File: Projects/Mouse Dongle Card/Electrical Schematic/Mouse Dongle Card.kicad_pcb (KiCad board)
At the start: 2 copper layers, 26 x 27.9 mm, 11 parts, among them P1 USB_C_Plug_USB2.0, U1 AP2112K-3.3

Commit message: Started work on USB Dongle Card
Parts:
- removed C2: 10uF, Capacitor_SMD:C_0805_2012Metric
- removed R1: 5.1k, Resistor_SMD:R_0603_1608Metric
- removed U1: AP2112K-3.3, Package_TO_SOT_SMD:SOT-23-5
- added R2: 5.1k, Resistor_SMD:R_1206_3216Metric_Pad1.30x1.75mm_HandSolder, F.Cu at (100.1, 123.5)
- added USBSolder1: ~, Connector_USB_PCB_Edge:USB_A_PCB_Edge_receptacle, B.Cu at (108.3, 128.6)
- C1: value 10uF -> 10nF; footprint Capacitor_SMD:C_0805_2012Metric -> Capacitor_SMD:C_1206_3216Metric_Pad1.33x1.80mm_HandSolder
- P1: value USB_C_Plug_USB2.0 -> USB_C_Plug
- moved C1 3.16 mm to (98.8, 131.9), turned to 0 degrees
- moved GP1 2.00 mm to (102.6, 122.0)
- moved GP2 2.00 mm to (102.6, 122.0)
- moved GP3 2.00 mm to (114.0, 122.0)
- moved GP4 2.00 mm to (114.0, 122.0)
- moved H1 2.00 mm to (97.0, 140.5)
- moved H2 2.00 mm to (119.6, 140.5)
- moved P1 2.00 mm to (108.3, 123.0)
- renumbered TP1 to GP1, TP2 to GP2, TP3 to GP3, TP4 to GP4
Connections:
- P1 pad A10: (no net) -> unconnected-(P1-RX2--PadA10)
- P1 pad A11: (no net) -> unconnected-(P1-RX2+-PadA11)
- P1 pad A2: (no net) -> /USB_TX1+
- P1 pad A3: (no net) -> /USB_TX1-
- P1 pad A6: (no net) -> /USB_DP
- P1 pad A7: (no net) -> /USB_DN
- P1 pad A8: (no net) -> unconnected-(P1-SBU1-PadA8)
- P1 pad B10: (no net) -> /USB_RX1-
- P1 pad B11: (no net) -> /USB_RX1+
- P1 pad B2: (no net) -> unconnected-(P1-TX2+-PadB2)
- P1 pad B3: (no net) -> unconnected-(P1-TX2--PadB3)
- P1 pad B5: (no net) -> unconnected-(P1-VCONN-PadB5)
- P1 pad B8: (no net) -> unconnected-(P1-SBU2-PadB8)
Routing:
- net GND: track 0.00 -> 21.6 mm
- net VBUS: track 0.00 -> 15.9 mm
- net /USB_DP: track 0.00 -> 10.6 mm, vias 0 -> 1
- net /USB_DN: track 0.00 -> 10.6 mm, vias 0 -> 1
- net Net-(P1-CC): track 0.00 -> 10.4 mm
- net /USB_RX1+: track 0.00 -> 0.79 mm
- net /USB_RX1-: track 0.00 -> 0.79 mm
- added copper zone on B.Cu, net GND
- added copper zone on F.Cu, net VBUS

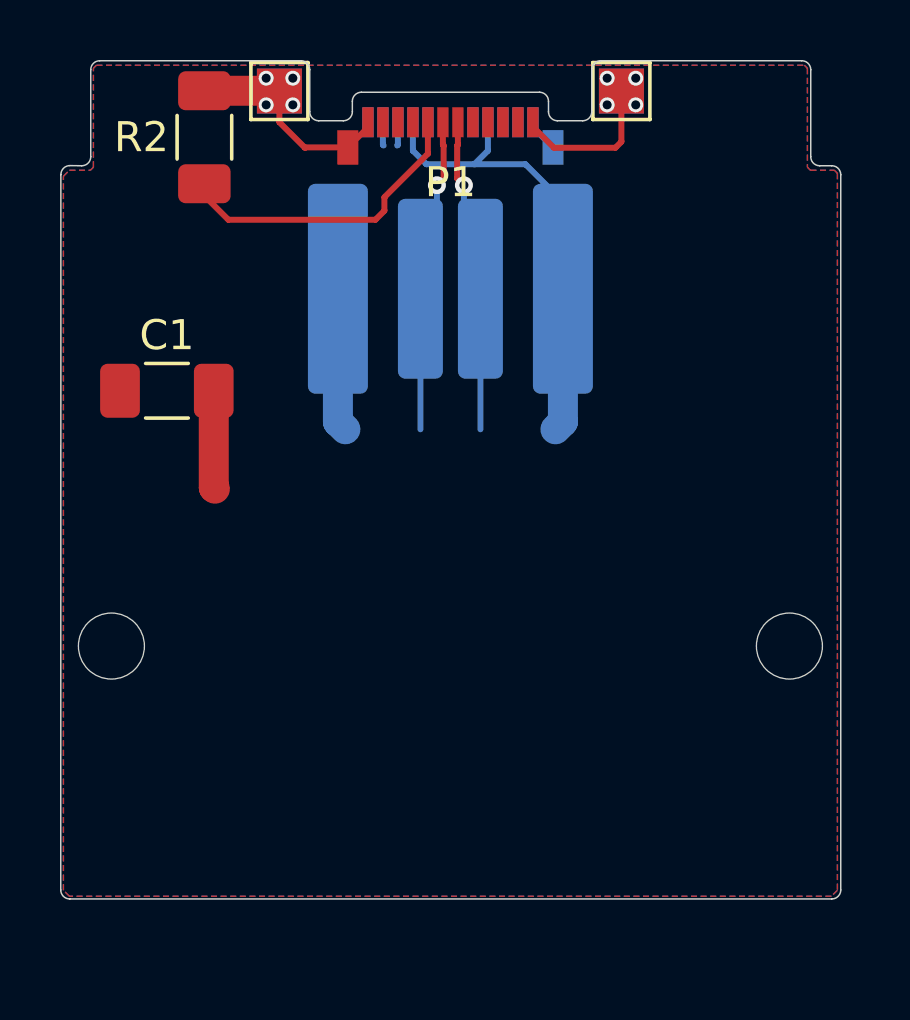
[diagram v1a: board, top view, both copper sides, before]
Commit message: Moved USB port and added OV bypass
Moved USB port on dongle card with preliminary offset. Will update when I have the ports on hand.
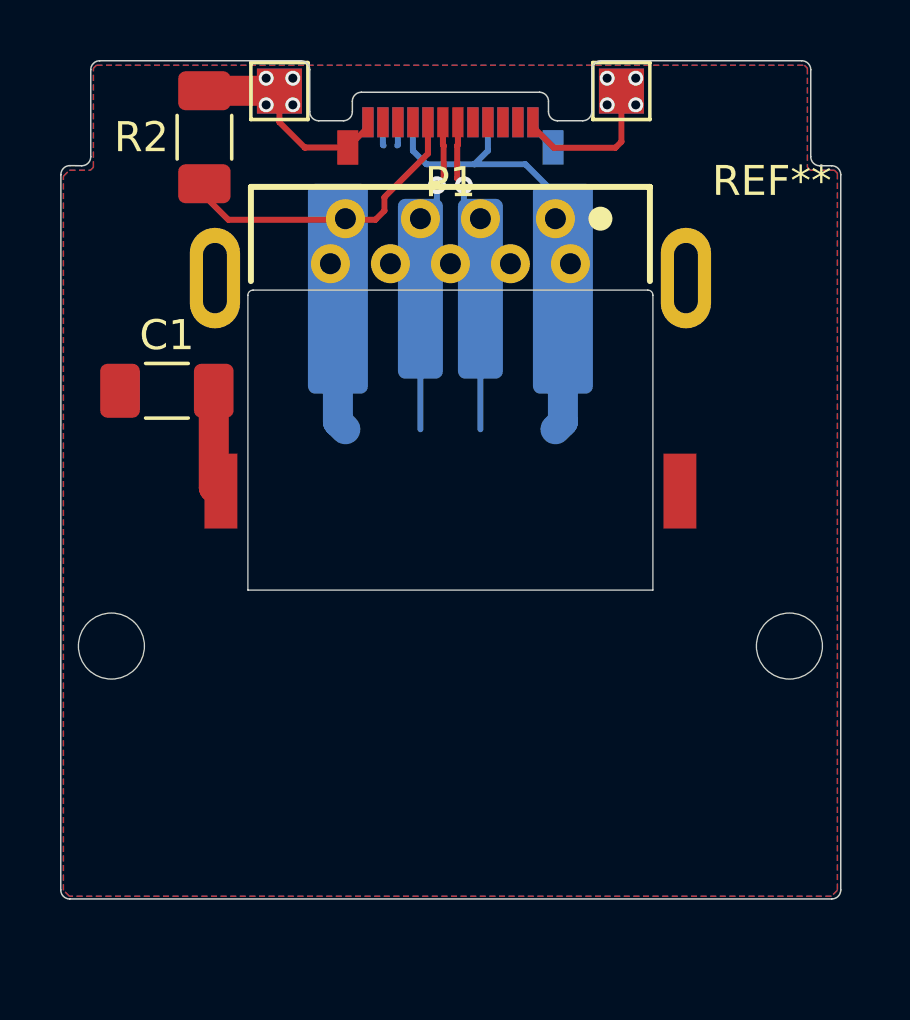
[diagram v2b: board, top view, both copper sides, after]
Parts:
- added REF**: 692121330100, Inset USB:692121330100, F.Cu at (108.3, 133.4)
